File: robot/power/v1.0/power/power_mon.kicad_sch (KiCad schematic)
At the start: 43 parts, among them J12 Conn_01x02, U11 AD8494

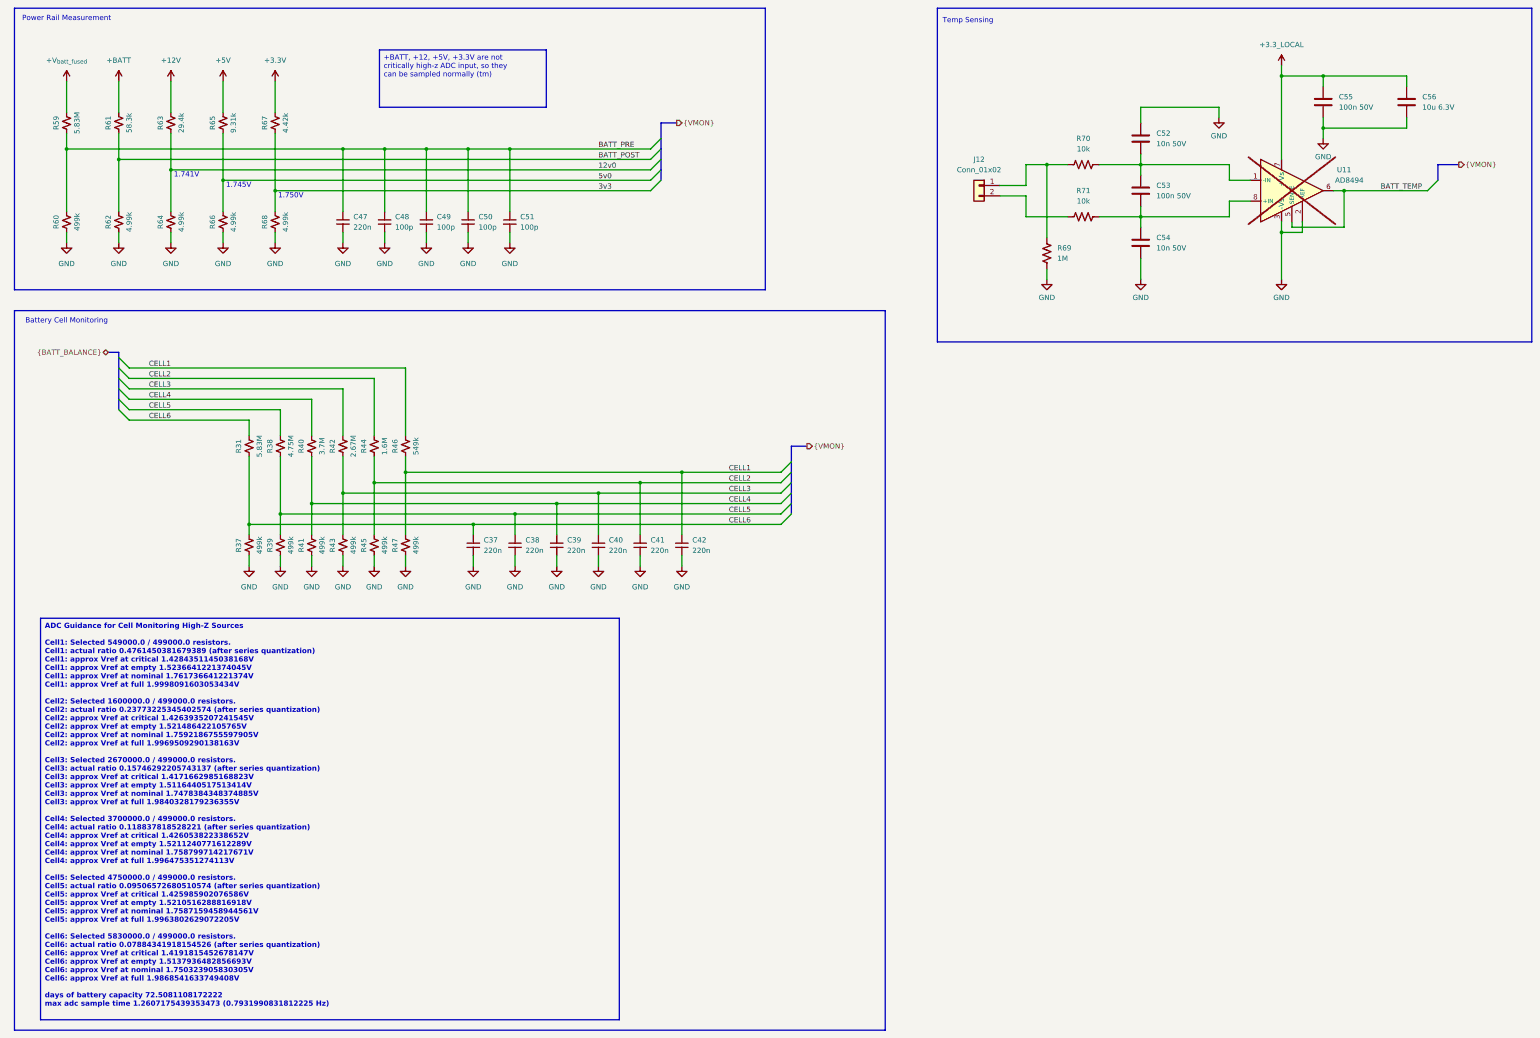
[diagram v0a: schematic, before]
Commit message: passing ERC, footprint work
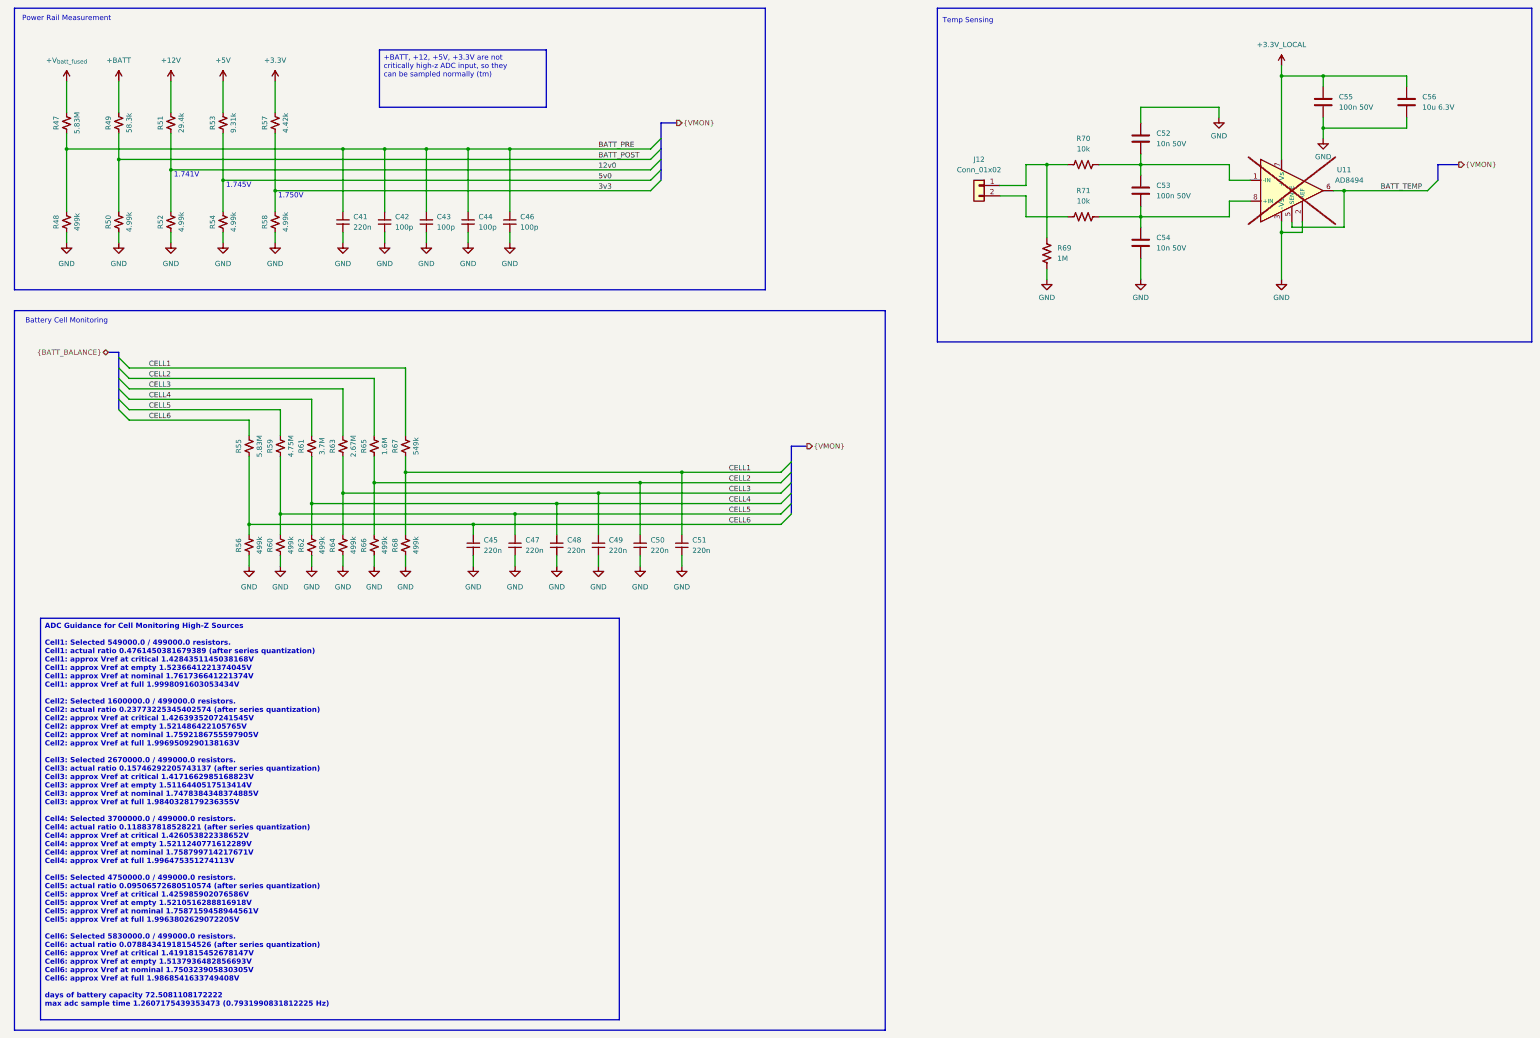
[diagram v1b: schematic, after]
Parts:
- R47: renamed from R59; footprint Resistor_SMD:R_0603_1608Metric -> Resistor_SMD:R_0402_1005Metric
- R48: renamed from R60; footprint Resistor_SMD:R_0603_1608Metric -> Resistor_SMD:R_0402_1005Metric
- R49: renamed from R61; footprint Resistor_SMD:R_0603_1608Metric -> Resistor_SMD:R_0402_1005Metric
- R50: renamed from R62; footprint Resistor_SMD:R_0603_1608Metric -> Resistor_SMD:R_0402_1005Metric
- R51: renamed from R63; footprint Resistor_SMD:R_0603_1608Metric -> Resistor_SMD:R_0402_1005Metric
- R52: renamed from R64; footprint Resistor_SMD:R_0603_1608Metric -> Resistor_SMD:R_0402_1005Metric
- R53: renamed from R65; footprint Resistor_SMD:R_0603_1608Metric -> Resistor_SMD:R_0402_1005Metric
- R54: renamed from R66; footprint Resistor_SMD:R_0603_1608Metric -> Resistor_SMD:R_0402_1005Metric
- R55: renamed from R31; footprint Resistor_SMD:R_0603_1608Metric -> Resistor_SMD:R_0402_1005Metric
- R56: renamed from R37; footprint Resistor_SMD:R_0603_1608Metric -> Resistor_SMD:R_0402_1005Metric
- R57: renamed from R67; footprint Resistor_SMD:R_0603_1608Metric -> Resistor_SMD:R_0402_1005Metric
- R58: renamed from R68; footprint Resistor_SMD:R_0603_1608Metric -> Resistor_SMD:R_0402_1005Metric
- R59: renamed from R38; footprint Resistor_SMD:R_0603_1608Metric -> Resistor_SMD:R_0402_1005Metric
- R60: renamed from R39; footprint Resistor_SMD:R_0603_1608Metric -> Resistor_SMD:R_0402_1005Metric
- R61: renamed from R40; footprint Resistor_SMD:R_0603_1608Metric -> Resistor_SMD:R_0402_1005Metric
- R62: renamed from R41; footprint Resistor_SMD:R_0603_1608Metric -> Resistor_SMD:R_0402_1005Metric
- R63: renamed from R42; footprint Resistor_SMD:R_0603_1608Metric -> Resistor_SMD:R_0402_1005Metric
- R64: renamed from R43; footprint Resistor_SMD:R_0603_1608Metric -> Resistor_SMD:R_0402_1005Metric
- R65: renamed from R44; footprint Resistor_SMD:R_0603_1608Metric -> Resistor_SMD:R_0402_1005Metric
- R66: renamed from R45; footprint Resistor_SMD:R_0603_1608Metric -> Resistor_SMD:R_0402_1005Metric
- R67: renamed from R46; footprint Resistor_SMD:R_0603_1608Metric -> Resistor_SMD:R_0402_1005Metric
- R68: renamed from R47; footprint Resistor_SMD:R_0603_1608Metric -> Resistor_SMD:R_0402_1005Metric
- renumbered C47 to C41, C48 to C42, C49 to C43, C50 to C44, C37 to C45, C51 to C46, C38 to C47, C39 to C48, C40 to C49, C41 to C50, C42 to C51
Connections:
- net +3.3_LOCAL renamed +3.3V_LOCAL

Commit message: power board passing ERC/import
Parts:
- C56: footprint Capacitor_SMD:C_0402_1005Metric -> Capacitor_SMD:C_1210_3225Metric
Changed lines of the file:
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@@
 			)
 		)
-		(property "Footprint" "Capacitor_SMD:C_0402_1005Metric"
+		(property "Footprint" "Capacitor_SMD:C_1210_3225Metric"
 			(at 354.6348 35.56 0)
 			(effects

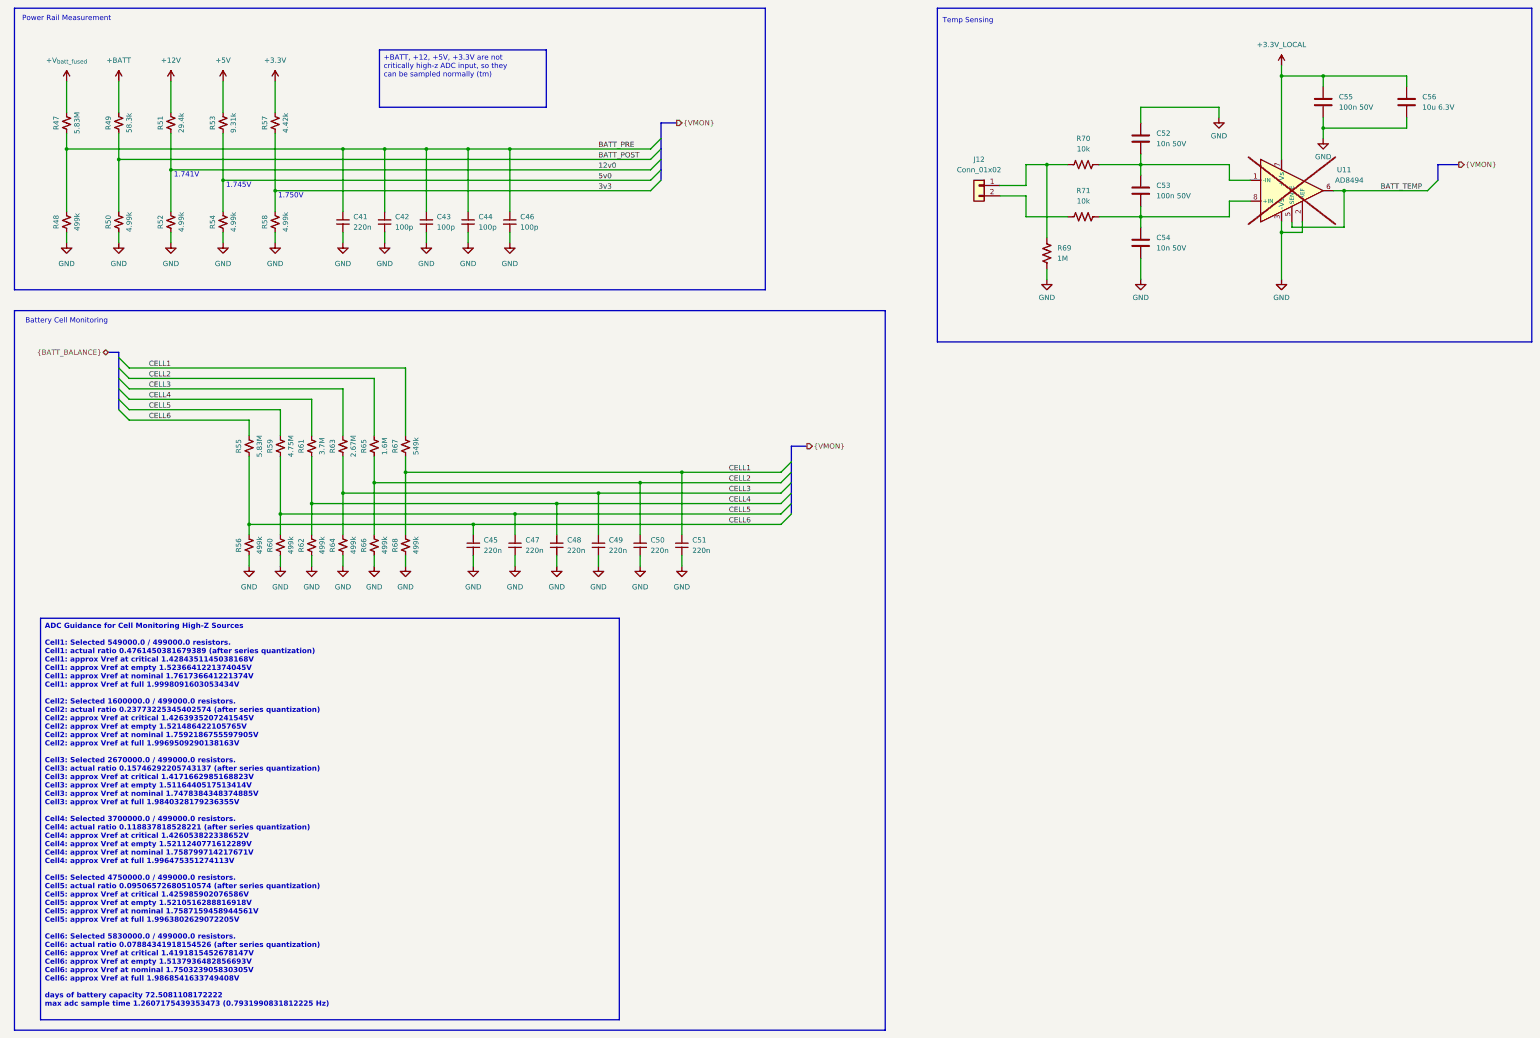
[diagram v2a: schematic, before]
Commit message: fix bus aliasing issues
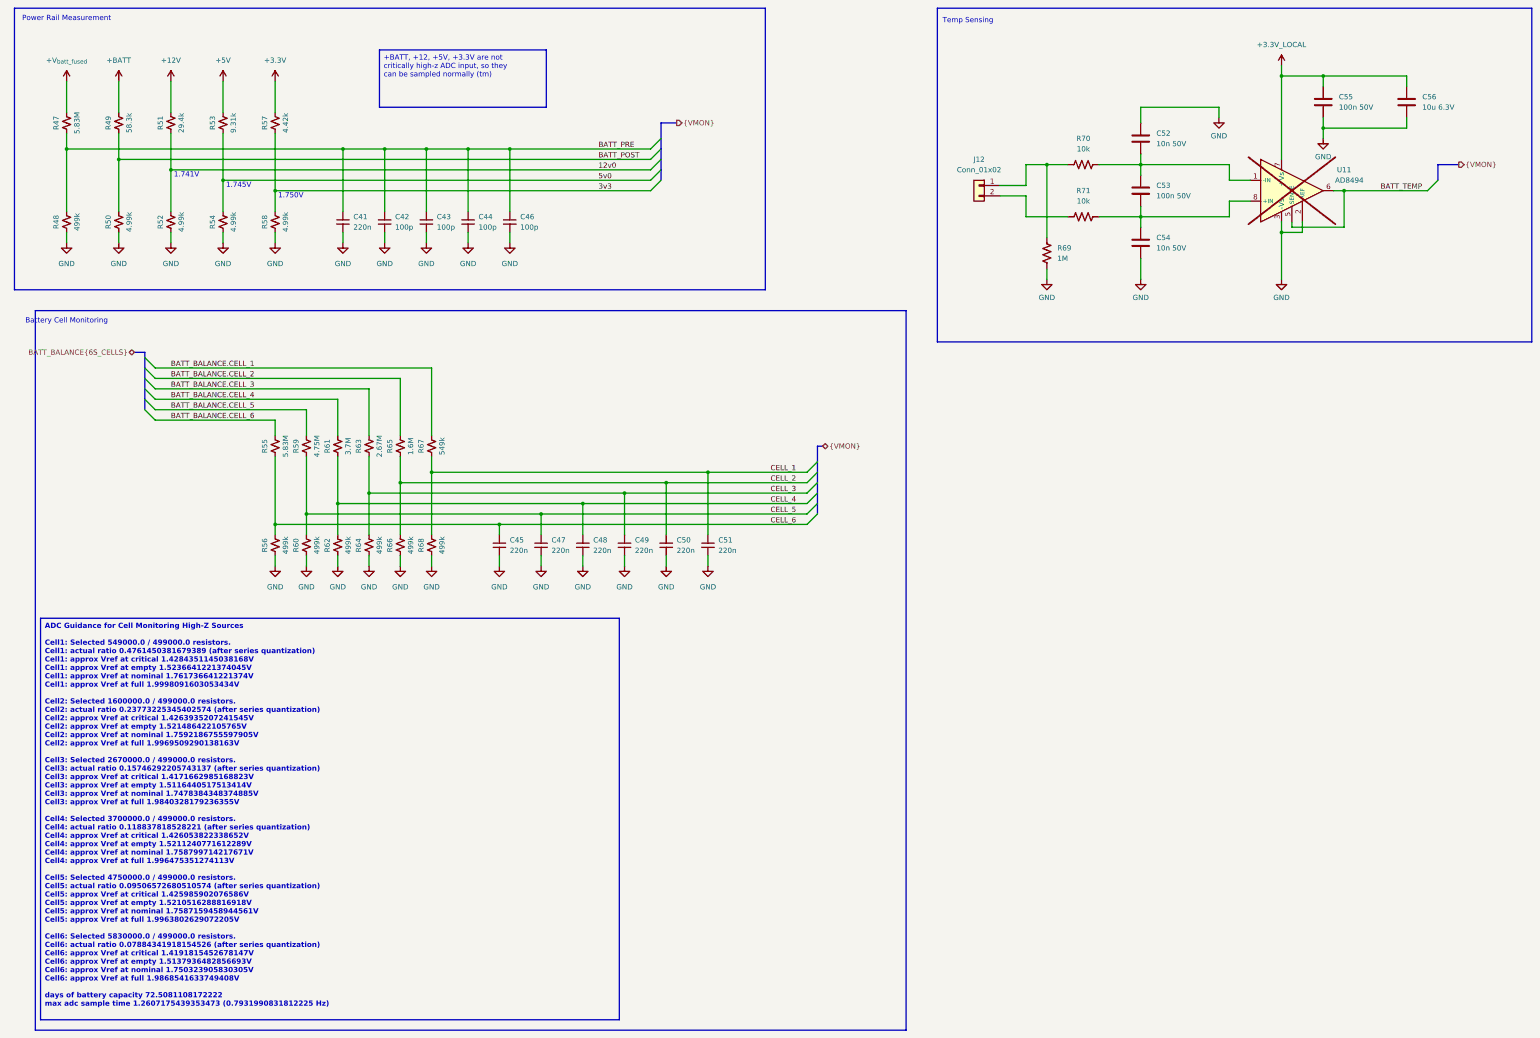
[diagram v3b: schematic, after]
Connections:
- net CELL1 renamed CELL_1
- net CELL_1: no longer R67.1
- net CELL2 renamed CELL_2
- net CELL_2: no longer R65.1
- net CELL3 renamed CELL_3
- net CELL_3: no longer R63.1
- net CELL4 renamed CELL_4
- net CELL_4: no longer R61.1
- net CELL5 renamed CELL_5
- net CELL_5: no longer R59.1
- net CELL6 renamed CELL_6
- net CELL_6: no longer R55.1
- new net BATT_BALANCE.CELL_1: R67.1
- new net BATT_BALANCE.CELL_2: R65.1
- new net BATT_BALANCE.CELL_3: R63.1
- new net BATT_BALANCE.CELL_4: R61.1
- new net BATT_BALANCE.CELL_5: R59.1
- new net BATT_BALANCE.CELL_6: R55.1
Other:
- moved on the sheet: C45, C47, C48, C49, C50, C51, R55, R56, R59, R60, R61, R62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

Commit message: layout work
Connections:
- net at R69.2, R70.1: now also J12.2 (Pin_2); no longer J12.1 (Pin_1)
- net at R71.1: now also J12.1 (Pin_1); no longer J12.2 (Pin_2)
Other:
- note added: "Swap makes routing easier"
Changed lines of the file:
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@@
-		)
-	)
-	(wire
-		(pts
-			(xy 262.89 62.23) (xy 262.89 67.31)
-		)
-		(stroke
-			(width 0)
-			(type default)
 		)
 	)
@@
 	(wire
 		(pts
-			(xy 256.54 59.69) (xy 262.89 59.69)
-		)
-		(stroke
-			(width 0)
-			(type default)
-		)
-	)
-	(wire
-		(pts
 			(xy 106.68 50.8) (xy 106.68 66.04)
 		)
@@
 	(wire
 		(pts
+			(xy 256.54 59.69) (xy 261.62 59.69)
+		)
+		(stroke
+			(width 0)
+			(type default)
+		)
+	)
+	(wire
+		(pts
 			(xy 80.01 125.73) (xy 80.01 142.24)
 		)
@@
 	(wire
 		(pts
+			(xy 256.54 62.23) (xy 262.89 62.23)
+		)
+		(stroke
+			(width 0)
+			(type default)
+		)
+	)
+	(wire
+		(pts
 			(xy 185.42 149.86) (xy 185.42 152.4)
 		)
@@
 	(wire
 		(pts
-			(xy 256.54 62.23) (xy 262.89 62.23)
-		)
-		(stroke
-			(width 0)
-			(type default)
-		)
-	)
-	(wire
-		(pts
 			(xy 290.83 54.61) (xy 290.83 57.15)
 		)
@@
 	(wire
 		(pts
+			(xy 261.62 59.69) (xy 261.62 67.31)
+		)
+		(stroke
+			(width 0)
+			(type default)
+		)
+	)
+	(wire
+		(pts
 			(xy 67.31 58.42) (xy 67.31 66.04)
 		)
@@
 	(wire
 		(pts
-			(xy 262.89 67.31) (xy 273.05 67.31)
+			(xy 261.62 67.31) (xy 273.05 67.31)
 		)
 		(stroke
@@
 	(wire
 		(pts
-			(xy 262.89 59.69) (xy 262.89 54.61)
+			(xy 262.89 54.61) (xy 262.89 62.23)
 		)
 		(stroke
@@
 		)
 	)
+	(text "Swap makes routing easier"
+		(exclude_from_sim no)
+		(at 259.08 46.99 0)
+		(effects
+			(font
+				(size 1.27 1.27)
+			)
+		)
+	)
 	(text "1.750V"
 		(exclude_from_sim no)
@@
 	(label "CELL_6"
 		(at 200.66 142.24 0)
+		(fields_autoplaced yes)
 		(effects
 			(font
@@
 	(label "BATT_BALANCE.CELL_6"
 		(at 54.61 116.84 0)
+		(fields_autoplaced yes)
 		(effects
 			(font
@@
 	(label "BATT_BALANCE.CELL_2"
 		(at 54.61 106.68 0)
+		(fields_autoplaced yes)
 		(effects
 			(font
@@
 	(label "BATT_BALANCE.CELL_1"
 		(at 54.61 104.14 0)
+		(fields_autoplaced yes)
 		(effects
 			(font
@@
 	(label "BATT_BALANCE.CELL_4"
 		(at 54.61 111.76 0)
+		(fields_autoplaced yes)
 		(effects
 			(font
@@
 	(label "BATT_BALANCE.CELL_5"
 		(at 54.61 114.3 0)
+		(fields_autoplaced yes)
 		(effects
 			(font
@@
 	(label "CELL_5"
 		(at 200.66 139.7 0)
+		(fields_autoplaced yes)
 		(effects
 			(font
@@
 	(label "CELL_4"
 		(at 200.66 137.16 0)
+		(fields_autoplaced yes)
 		(effects
 			(font
@@
 	(label "CELL_1"
 		(at 200.66 129.54 0)
+		(fields_autoplaced yes)
 		(effects
 			(font
@@
 	(label "BATT_BALANCE.CELL_3"
 		(at 54.61 109.22 0)
+		(fields_autoplaced yes)
 		(effects
 			(font
@@
 	(label "CELL_3"
 		(at 200.66 134.62 0)
+		(fields_autoplaced yes)
 		(effects
 			(font
@@
 	(label "CELL_2"
 		(at 200.66 132.08 0)
-		(effects
-			(font
+		(fields_autoplaced yes)
+		(effects
+			(font

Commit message: initial placement
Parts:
- renumbered C41 to C45, C42 to C46, C43 to C47, C44 to C48, C45 to C49, C46 to C50, C47 to C51, C48 to C52, C49 to C53, C50 to C54, C51 to C55, C52 to C56, C53 to C57, C54 to C58, C55 to C59, C56 to C60, J12 to J9, R47 to R50, R48 to R51, R49 to R52, R50 to R53, R51 to R54, R52 to R55, R53 to R56, R54 to R57, R57 to R58, R58 to R59, R55 to R60, R56 to R61, R59 to R62, R60 to R63, R61 to R64, R62 to R65, R63 to R66, R64 to R67, R65 to R68, R66 to R69, R67 to R70, R68 to R71, R69 to R72, R70 to R73, R71 to R74
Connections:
- net 12v0: now also C47.1
- net 3v3: now also C50.1
- net 5v0: now also C48.1
- net BATT_POST: now also C46.1
- net BATT_PRE: no longer C46.1, C47.1, C48.1, C50.1
